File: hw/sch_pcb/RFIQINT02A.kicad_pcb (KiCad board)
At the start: 2 copper layers, 40.1 x 60.5 mm, 36 parts, among them J1 HEADER_2x03_PARALLEL, J2 HEADER_2x04_PARALLEL, J3 SATA7-67491-1030, J4 SATA7-67491-1030, J5 SATA7-67491-1030, J6 RJ45_RJHSE-5384, J7 RJ45_RJHSE-5384, M1 HOLE, M2 HOLE, M3 HOLE, M4 HOLE, U1 Si53322

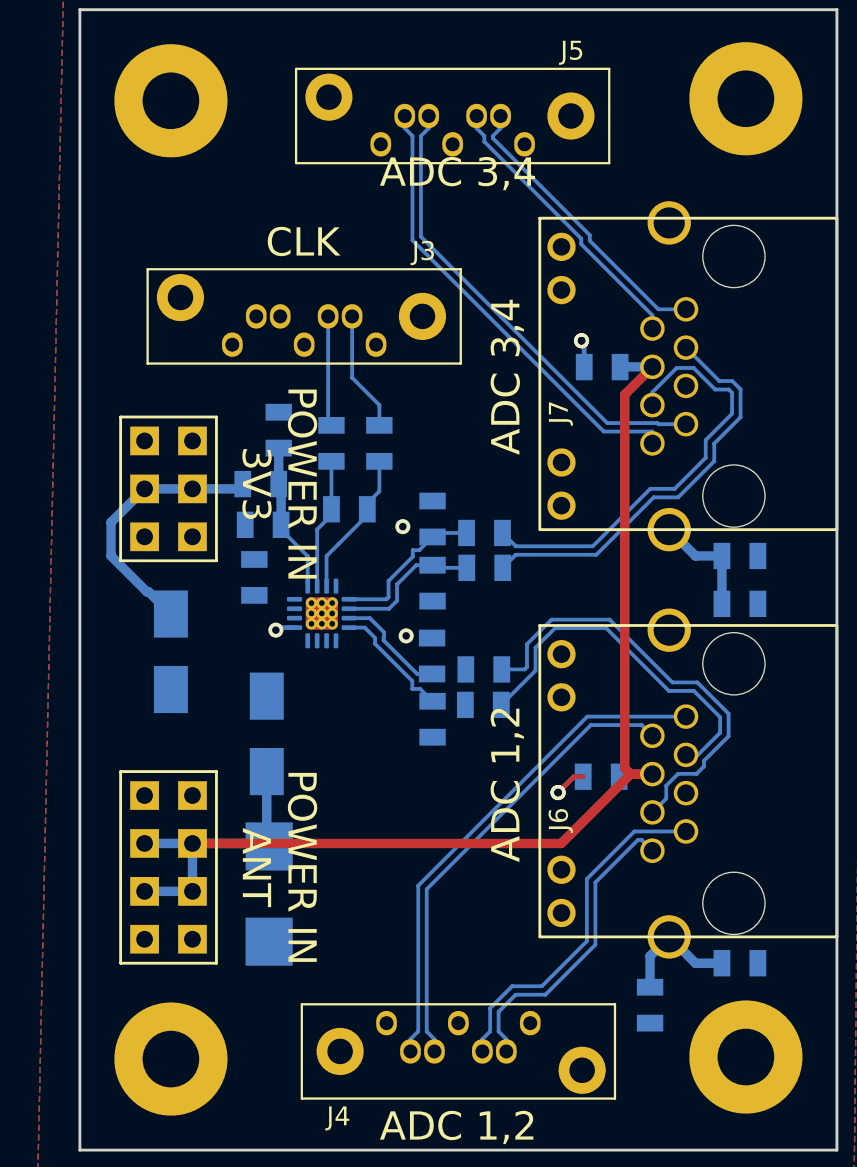
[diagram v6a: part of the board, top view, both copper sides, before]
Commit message: Apply net class parameters.
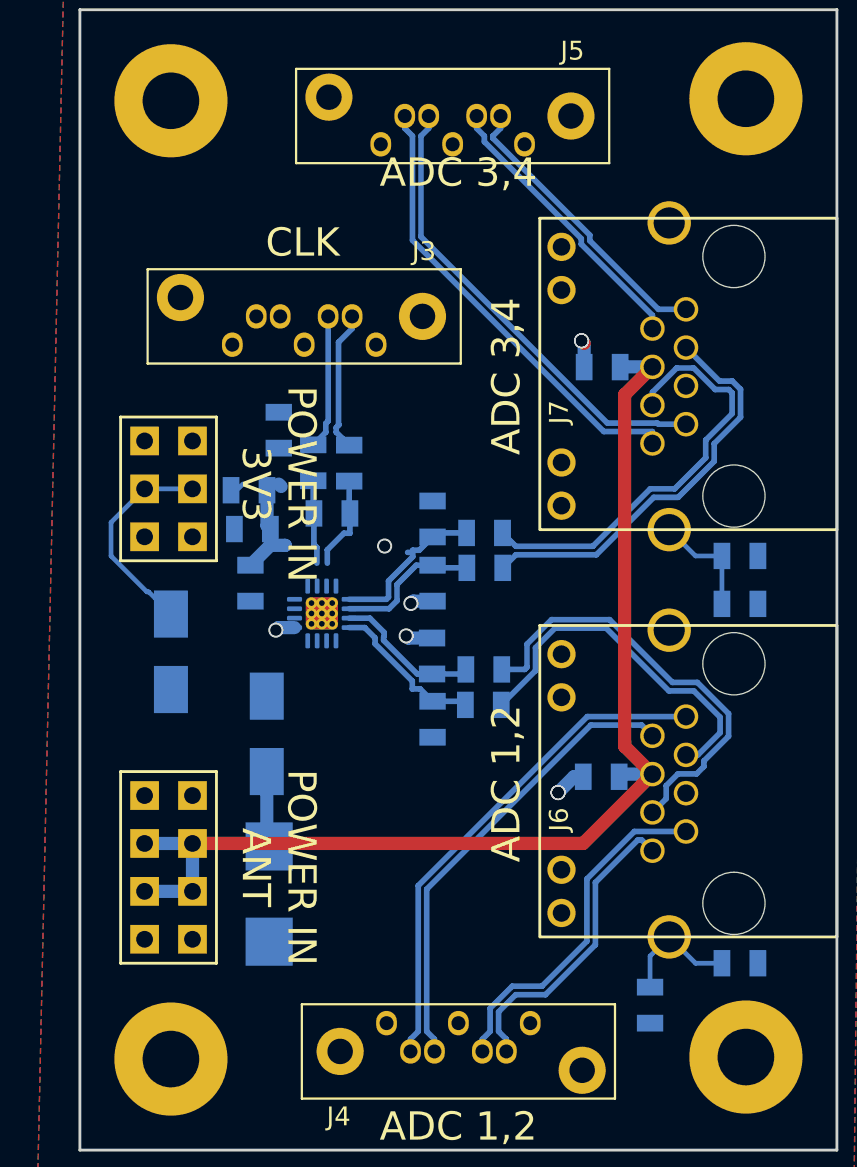
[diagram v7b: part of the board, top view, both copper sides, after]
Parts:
- moved C5 3.17 mm to (9.30, -30.2), turned to -90 degrees
- moved C14 2.57 mm to (9.40, -33.1), turned to 180 degrees
- moved C4 1.91 mm to (14.5, -36.6)
- moved C3 1.41 mm to (12.6, -36.6)
- moved R1 0.95 mm to (13.6, -33.9)
- moved L1 0.70 mm to (9.22, -35.1)
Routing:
- net /CLK_N: track 7.77 -> 5.05 mm
- net +3V3: track 7.95 -> 5.47 mm
- net /CLK_P: track 6.93 -> 4.45 mm
- net Net-(D1-Pad1): track 14.1 -> 11.6 mm
- net /CLKIN_N: track 6.38 -> 8.61 mm
- net /Q1_P: track 5.86 -> 7.75 mm
- net /Q1_N: track 6.42 -> 8.24 mm
- net /CLKIN_P: track 6.17 -> 7.70 mm
- net GND: track 6.06 -> 6.99 mm, vias 7 -> 8

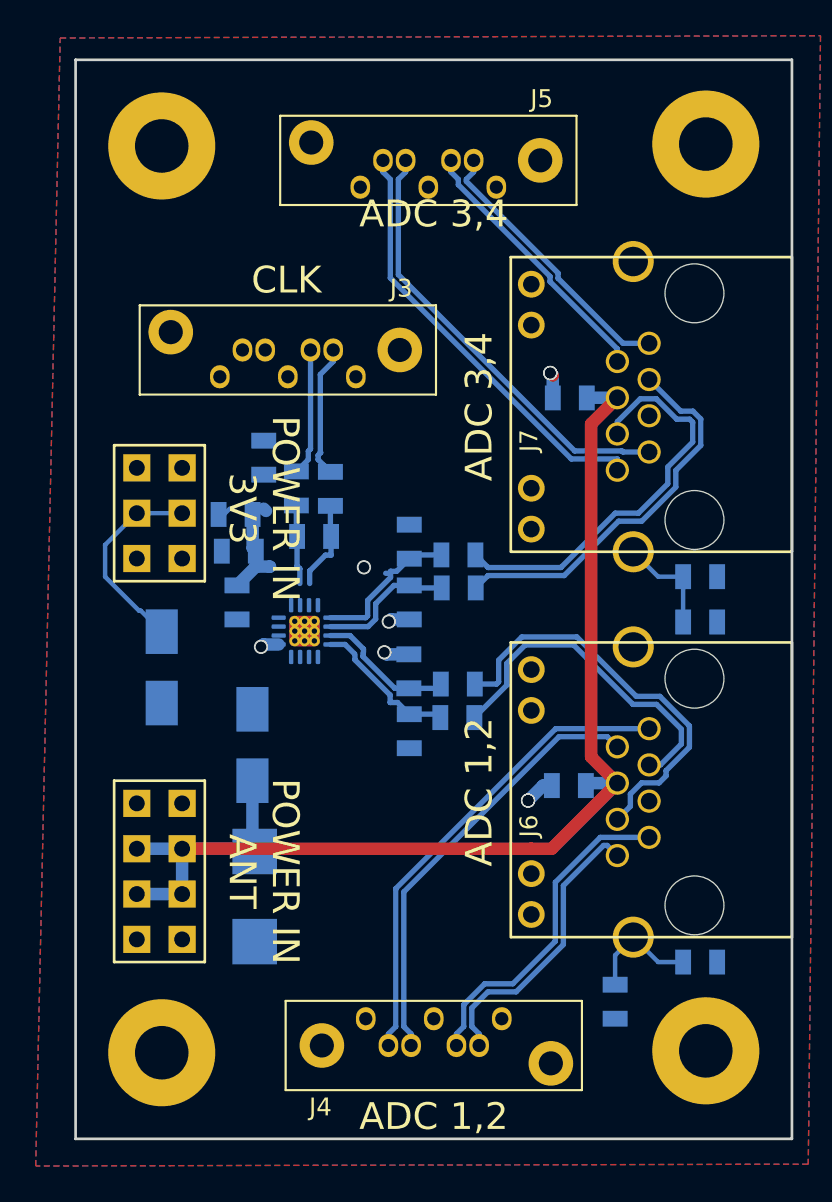
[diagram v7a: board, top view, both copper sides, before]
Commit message: Tune skew of differential pairs.
Use the RJ45 connector's LED as power indicators.
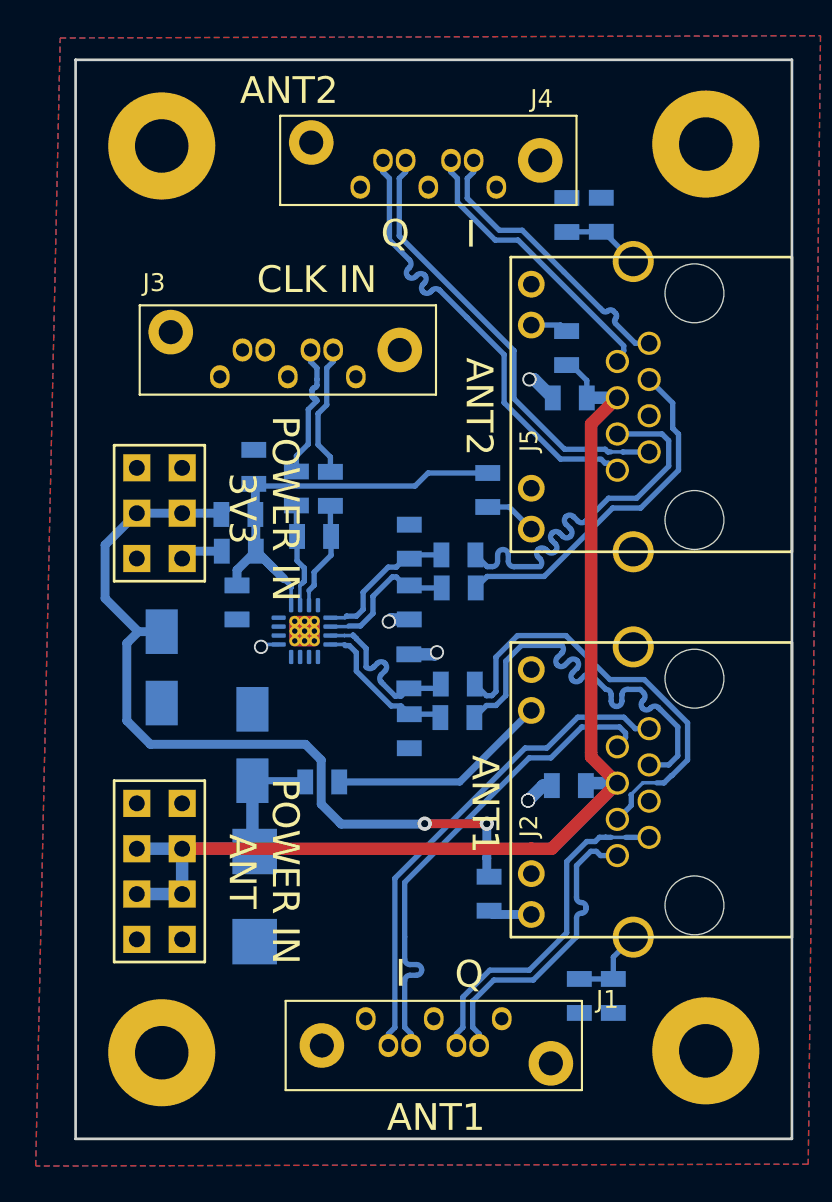
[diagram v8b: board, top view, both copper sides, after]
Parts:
- added R1: 1k, Mlab_R:SMD-0805, B.Cu at (14.1, -20.1)
- added R10: 1k, Mlab_R:SMD-0805, B.Cu at (23.3, -36.5)
- added R2: 1k, Mlab_R:SMD-0805, B.Cu at (23.4, -13.9)
- added R9: 1k, Mlab_R:SMD-0805, B.Cu at (27.8, -44.5)
- moved C12 23.5 mm to (29.7, -51.9), turned to 90 degrees
- moved R11 21.6 mm to (27.8, -51.9), turned to 90 degrees
- moved R3 7.03 mm to (28.5, -8.15), turned to -90 degrees
- moved C13 0.76 mm to (10.2, -37.8)
- moved C7 0.34 mm to (30.4, -8.15)
- moved L1 0.15 mm to (9.37, -35.1)
- renumbered C12 to C1, C4 to C10, C13 to C11, C11 to C12, C2 to C13, C1 to C14, C14 to C2, C5 to C3, C6 to C4, C3 to C5, C7 to C6, C10 to C7, J4 to J1, J6 to J2, J5 to J4, J7 to J5, J1 to J6, J2 to J7, R7 to R11, R6 to R3, R1 to R4, R2 to R5, R3 to R6, R4 to R7, R5 to R8
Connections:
- net Net-(D1-Pad1) renamed +3V8
- C12 pad 1: Net-(C11-Pad1) -> Net-(C12-Pad1)
- J2 pad 10: unconnected-(J6-Pad10) -> Net-(J2-Pad10)
- J2 pad 11: unconnected-(J6-Pad11) -> GND
- J2 pad 12: unconnected-(J6-Pad12) -> Net-(J2-Pad12)
- J2 pad 9: unconnected-(J6-Pad9) -> GND
- J5 pad 10: unconnected-(J7-Pad10) -> Net-(J5-Pad10)
- J5 pad 11: unconnected-(J7-Pad11) -> GND
- J5 pad 12: unconnected-(J7-Pad12) -> Net-(J5-Pad12)
- J5 pad 13: Net-(C11-Pad1) -> unconnected-(J5-Pad13)
- J5 pad 14: (no net) -> Net-(C12-Pad1)
- J5 pad 9: unconnected-(J7-Pad9) -> GND
- R11 pad 1: Net-(C11-Pad1) -> Net-(C12-Pad1)
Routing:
- net +3V8: track 11.6 -> 46.7 mm, vias 0 -> 2
- net +3V3: track 5.47 -> 25.8 mm
- net Net-(J2-Pad10): track 0.00 -> 12.4 mm
- net Net-(C11-Pad1): track 5.91 -> 0.00 mm
- net VCC: track 68.0 -> 73.5 mm
- net /CLKOUT0_N: track 19.1 -> 24.3 mm
- net Net-(C12-Pad1): track 0.00 -> 4.42 mm
- net /ADC1_N: track 24.6 -> 27.7 mm
- net Net-(J5-Pad12): track 0.00 -> 2.96 mm
- net GND: track 6.99 -> 9.68 mm, vias 8 -> 6
- net Net-(J2-Pad12): track 0.00 -> 2.48 mm
- net Net-(J5-Pad10): track 0.00 -> 2.12 mm
- net /Q1_P: track 7.75 -> 9.83 mm
- net /CLKOUT1_N: track 21.9 -> 20.0 mm
- net Net-(C7-Pad1): track 6.46 -> 4.71 mm
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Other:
- board text added: "ANT1"
- board text added: "ANT2"
- board text added: "CLK IN"
- board text added: "I"
- board text added: "Q"
- board text removed: "ADC 1,2"
- board text removed: "ADC 3,4"
- board text removed: "CLK"
